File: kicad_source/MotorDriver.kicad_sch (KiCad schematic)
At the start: 44 parts, among them J7 x, J8 x, J9 x, Q1 2N7002, U4 74xx08, U5 IFX007T, U6 IFX007T, U7 IFX007T, U8 IFX007T

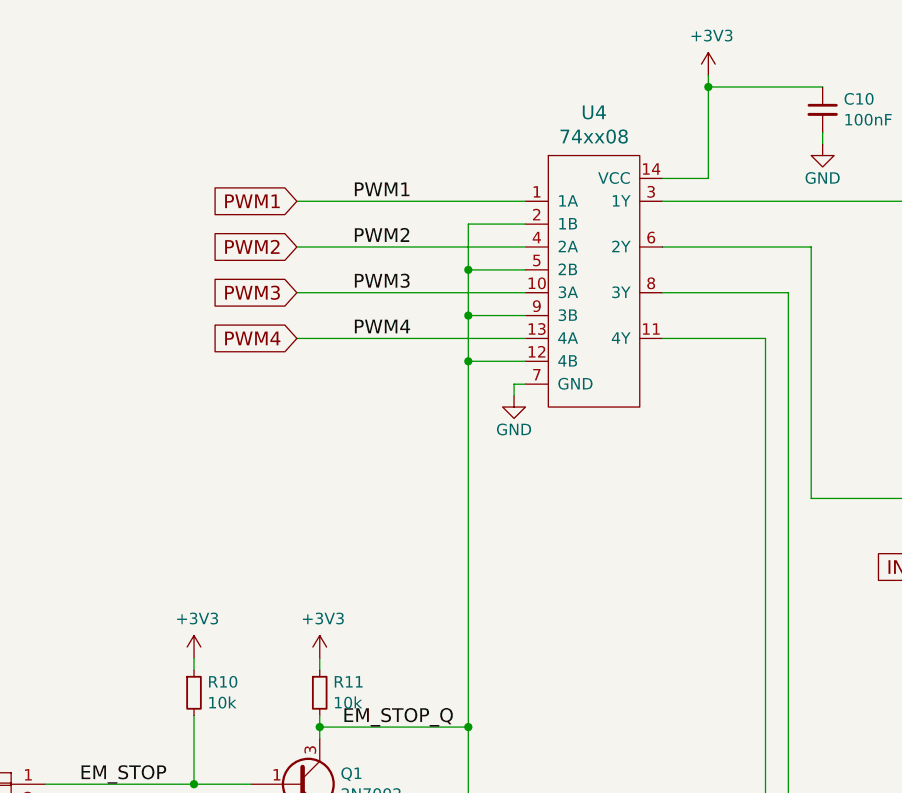
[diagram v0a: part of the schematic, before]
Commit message: combined 3.3V nets
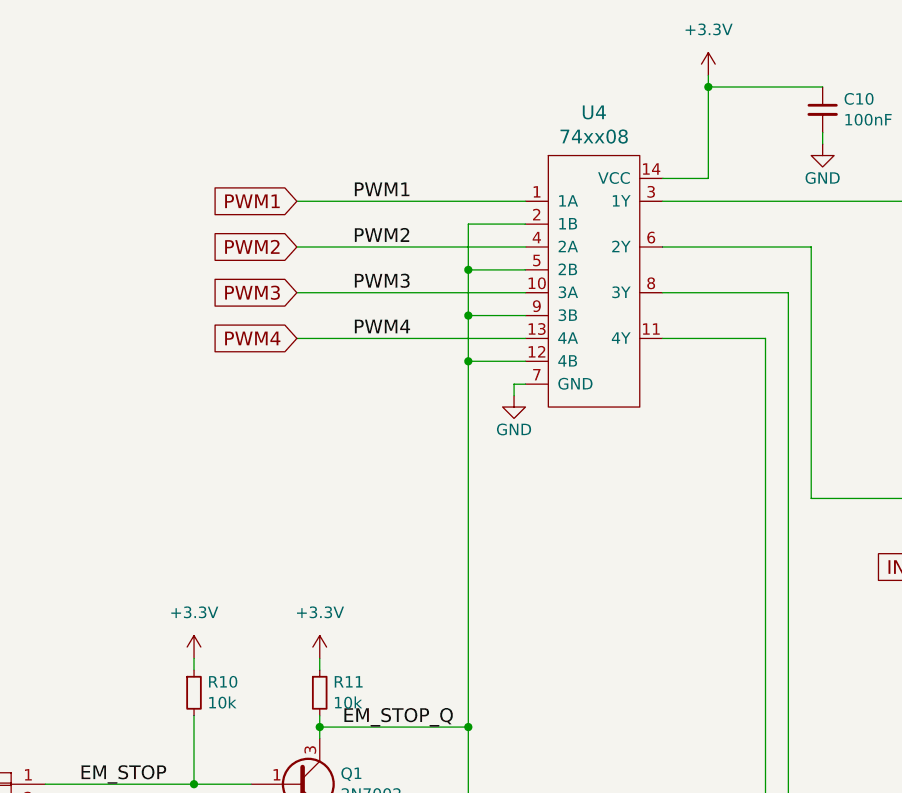
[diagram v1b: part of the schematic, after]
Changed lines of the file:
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@@
   (title_block
     (title "CyphalRobotController07/CAN")
-    (date "2023-11-15")
-    (rev "0.1")
+    (date "2023-12-03")
+    (rev "0.2")
     (company "generationmake")
     (comment 4 "This documentation describes Open Hardware and is licensed under the CERN OHL v. 1.2.")
@@
     (pin "1")
   )
-  (symbol (lib_id "power:+3.3V") (at 135.89 20.32 0) (unit 1)
-    (in_bom yes) (on_board yes)
-    (property "Reference" "#PWR048" (id 0) (at 135.89 24.13 0)
-      (effects (font (size 1.27 1.27)) hide)
-    )
-    (property "Value" "+3V3" (id 1) (at 136.271 15.9258 0))
-    (property "Footprint" "" (id 2) (at 135.89 20.32 0))
-    (property "Datasheet" "" (id 3) (at 135.89 20.32 0))
-    (pin "1")
-  )
   (symbol (lib_id "power:GND") (at 114.3 55.88 0) (unit 1)
     (in_bom yes) (on_board yes)
@@
     (pin "1")
   )
-  (symbol (lib_id "power:+3.3V") (at 92.71 85.09 0) (unit 1)
-    (in_bom yes) (on_board yes)
-    (property "Reference" "#PWR045" (id 0) (at 92.71 88.9 0)
-      (effects (font (size 1.27 1.27)) hide)
-    )
-    (property "Value" "+3V3" (id 1) (at 93.091 80.6958 0))
-    (property "Footprint" "" (id 2) (at 92.71 85.09 0))
-    (property "Datasheet" "" (id 3) (at 92.71 85.09 0))
-    (pin "1")
-  )
-  (symbol (lib_id "power:+3.3V") (at 78.74 85.09 0) (unit 1)
-    (in_bom yes) (on_board yes)
-    (property "Reference" "#PWR044" (id 0) (at 78.74 88.9 0)
-      (effects (font (size 1.27 1.27)) hide)
-    )
-    (property "Value" "+3V3" (id 1) (at 79.121 80.6958 0))
-    (property "Footprint" "" (id 2) (at 78.74 85.09 0))
-    (property "Datasheet" "" (id 3) (at 78.74 85.09 0))
-    (pin "1")
-  )
   (symbol (lib_id "OpenCyphalRobotController07-rescue:WR-TBL_691313710002-mechanical-connectors") (at 57.15 100.33 0) (mirror y) (unit 1)
     (in_bom yes) (on_board yes)
@@
     (pin "1")
   )
+  (symbol (lib_id "power:+3.3V") (at 92.71 85.09 0) (unit 1)
+    (in_bom yes) (on_board yes) (fields_autoplaced)
+    (property "Reference" "#PWR0134" (id 0) (at 92.71 88.9 0)
+      (effects (font (size 1.27 1.27)) hide)
+    )
+    (property "Value" "+3.3V" (id 1) (at 92.71 80.01 0))
+    (property "Footprint" "" (id 2) (at 92.71 85.09 0)
+      (effects (font (size 1.27 1.27)) hide)
+    )
+    (property "Datasheet" "" (id 3) (at 92.71 85.09 0)
+      (effects (font (size 1.27 1.27)) hide)
+    )
+    (pin "1")
+  )
   (symbol (lib_id "power:+BATT") (at 67.31 140.97 0) (unit 1)
     (in_bom yes) (on_board yes) (fields_autoplaced)
@@
     (pin "1")
   )
+  (symbol (lib_id "power:+3.3V") (at 78.74 85.09 0) (unit 1)
+    (in_bom yes) (on_board yes) (fields_autoplaced)
+    (property "Reference" "#PWR0101" (id 0) (at 78.74 88.9 0)
+      (effects (font (size 1.27 1.27)) hide)
+    )
+    (property "Value" "+3.3V" (id 1) (at 78.74 80.01 0))
+    (property "Footprint" "" (id 2) (at 78.74 85.09 0)
+      (effects (font (size 1.27 1.27)) hide)
+    )
+    (property "Datasheet" "" (id 3) (at 78.74 85.09 0)
+      (effects (font (size 1.27 1.27)) hide)
+    )
+    (pin "1")
+  )
   (symbol (lib_id "power:+BATT") (at 50.8 140.97 0) (unit 1)
     (in_bom yes) (on_board yes) (fields_autoplaced)
@@
       (effects (font (size 1.27 1.27)) hide)
     )
+    (pin "1")
+  )
+  (symbol (lib_id "power:+3.3V") (at 135.89 20.32 0) (unit 1)
+    (in_bom yes) (on_board yes) (fields_autoplaced)
+    (property "Reference" "#PWR0136" (id 0) (at 135.89 24.13 0)
+      (effects (font (size 1.27 1.27)) hide)
+    )
+    (property "Value" "+3.3V" (id 1) (at 135.89 15.24 0))
+    (property "Footprint" "" (id 2) (at 135.89 20.32 0)
+      (effects (font (size 1.27 1.27)) hide)
+    )
+    (property "Datasheet" "" (id 3) (at 135.89 20.32 0)
+      (effects (font (size 1.27 1.27)) hide)
+    )

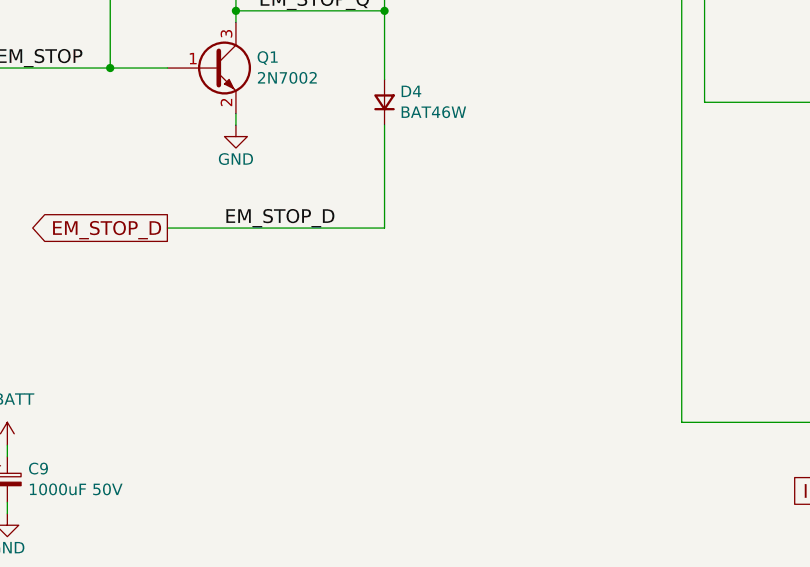
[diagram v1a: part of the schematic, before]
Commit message: added weak pull down on EM_STOP_D
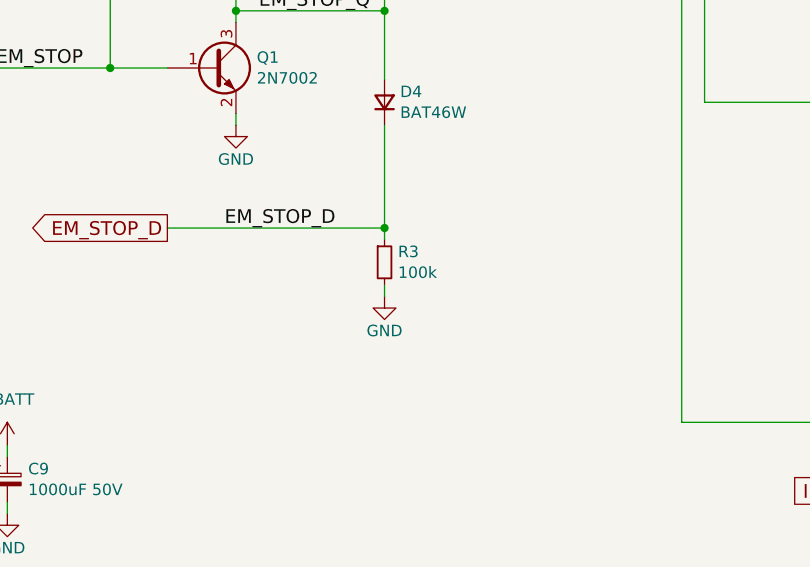
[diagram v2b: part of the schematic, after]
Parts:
- added R3: 100k, Resistor_SMD:R_0603_1608Metric, symbol Device:R_Small
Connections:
- net EM_STOP_D: now also R3.1
- net GND: now also R3.2
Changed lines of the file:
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@@
   (junction (at 92.71 92.71) (diameter 0) (color 0 0 0 0)
   )
+  (junction (at 109.22 116.84) (diameter 0) (color 0 0 0 0)
+  )
   (junction (at 189.23 149.86) (diameter 0) (color 0 0 0 0)
   )
@@
     (stroke (width 0) (type default) (color 0 0 0 0))
   )
+  (wire (pts (xy 109.22 123.19) (xy 109.22 124.46))
+    (stroke (width 0) (type default) (color 0 0 0 0))
+  )
   (wire (pts (xy 245.11 50.8) (xy 247.65 50.8))
     (stroke (width 0) (type default) (color 0 0 0 0))
@@
   )
   (wire (pts (xy 135.89 21.59) (xy 135.89 31.75))
+    (stroke (width 0) (type default) (color 0 0 0 0))
+  )
+  (wire (pts (xy 109.22 116.84) (xy 109.22 118.11))
     (stroke (width 0) (type default) (color 0 0 0 0))
   )
@@
     (pin "1")
   )
+  (symbol (lib_id "power:GND") (at 109.22 124.46 0) (unit 1)
+    (in_bom yes) (on_board yes)
+    (property "Reference" "#PWR020" (id 0) (at 109.22 130.81 0)
+      (effects (font (size 1.27 1.27)) hide)
+    )
+    (property "Value" "GND" (id 1) (at 109.22 128.27 0))
+    (property "Footprint" "" (id 2) (at 109.22 124.46 0))
+    (property "Datasheet" "" (id 3) (at 109.22 124.46 0))
+    (pin "1")
+  )
+  (symbol (lib_id "Device:R_Small") (at 109.22 120.65 0) (unit 1)
+    (in_bom yes) (on_board yes)
+    (property "Reference" "R3" (id 0) (at 110.7186 119.4816 0)
+      (effects (font (size 1.27 1.27)) (justify left))
+    )
+    (property "Value" "100k" (id 1) (at 110.7186 121.793 0)
+      (effects (font (size 1.27 1.27)) (justify left))
+    )
+    (property "Footprint" "Resistor_SMD:R_0603_1608Metric" (id 2) (at 109.22 124.46 0)
+      (effects (font (size 1.27 1.27)) hide)
+    )
+    (property "Datasheet" "" (id 3) (at 109.22 120.65 0))
+    (pin "1")
+    (pin "2")
+  )
   (symbol (lib_id "power:+3.3V") (at 78.74 85.09 0) (unit 1)

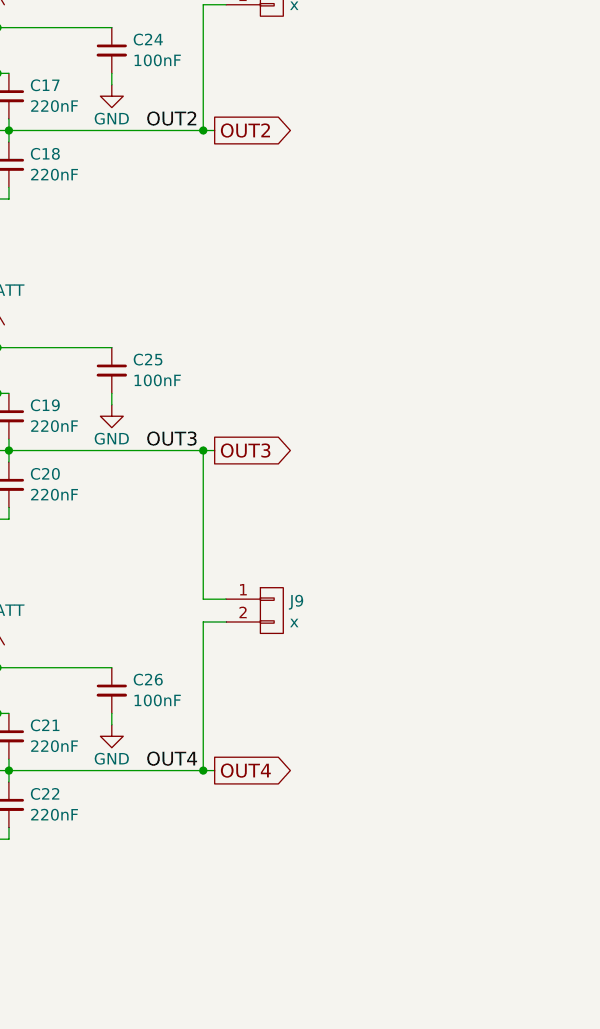
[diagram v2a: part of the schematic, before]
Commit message: added JST XH connector for motor and encoder
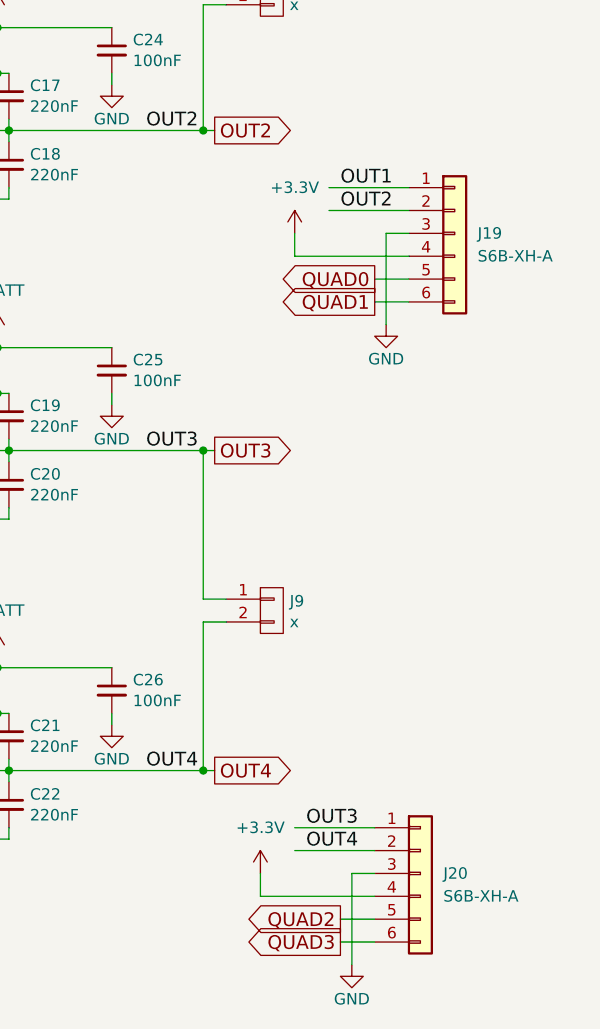
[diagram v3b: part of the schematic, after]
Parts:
- added J19, J20: S6B-XH-A, Connector_JST:JST_XH_S6B-XH-A_1x06_P2.50mm_Horizontal, symbol Connector_Generic:Conn_01x06
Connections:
- net +3.3V: now also J19.4 (Pin_4), J20.4 (Pin_4)
- net GND: now also J19.3 (Pin_3), J20.3 (Pin_3)
- net OUT1: now also J19.1 (Pin_1)
- net OUT2: now also J19.2 (Pin_2)
- net OUT3: now also J20.1 (Pin_1)
- net OUT4: now also J20.2 (Pin_2)
- new net QUAD0: J19.5 (Pin_5)
- new net QUAD1: J19.6 (Pin_6)
- new net QUAD2: J20.5 (Pin_5)
- new net QUAD3: J20.6 (Pin_6)

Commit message: changed motor connector, connected encoder
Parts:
- J8, J9: footprint Connector_Phoenix_MC:PhoenixContact_MC_1,5_2-G-3.81_1x02_P3.81mm_Horizontal -> Connector_Phoenix_MSTB:PhoenixContact_MSTBA_2,5_2-G-5,08_1x02_P5.08mm_Horizontal
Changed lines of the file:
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@@
   (title_block
     (title "CyphalRobotController07/CAN")
-    (date "2023-12-03")
+    (date "2024-01-04")
     (rev "0.2")
     (company "generationmake")
@@
       (effects (font (size 1.27 1.27)) (justify left))
     )
-    (property "Footprint" "Connector_Phoenix_MC:PhoenixContact_MC_1,5_2-G-3.81_1x02_P3.81mm_Horizontal" (id 2) (at 250.19 50.8 0)
+    (property "Footprint" "Connector_Phoenix_MSTB:PhoenixContact_MSTBA_2,5_2-G-5,08_1x02_P5.08mm_Horizontal" (id 2) (at 250.19 50.8 0)
       (effects (font (size 1.27 1.27)) hide)
     )
@@
       (effects (font (size 1.27 1.27)) (justify left))
     )
-    (property "Footprint" "Connector_Phoenix_MC:PhoenixContact_MC_1,5_2-G-3.81_1x02_P3.81mm_Horizontal" (id 2) (at 250.19 119.38 0)
-      (effects (font (size 1.27 1.27)) hide)
-    )
+    (property "Footprint" "Connector_Phoenix_MSTB:PhoenixContact_MSTBA_2,5_2-G-5,08_1x02_P5.08mm_Horizontal" (id 2) (at 250.19 119.38 0)
+      (effects (font (size 1.27 1.27)) hide)
+    )

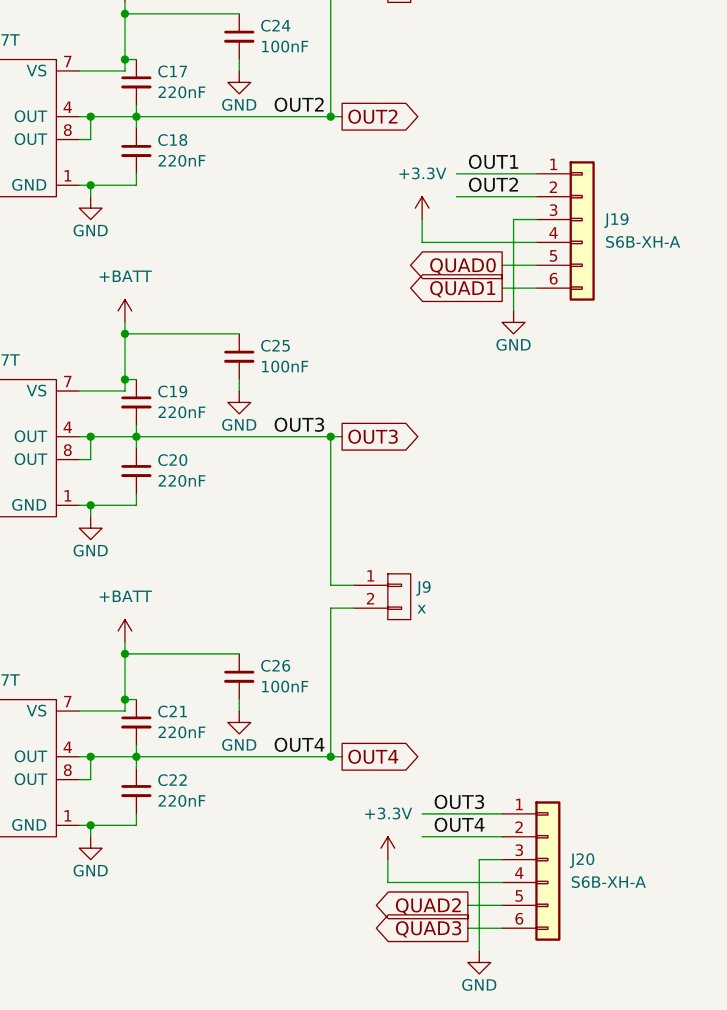
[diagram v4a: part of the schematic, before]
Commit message: finished layout near encoder level converter
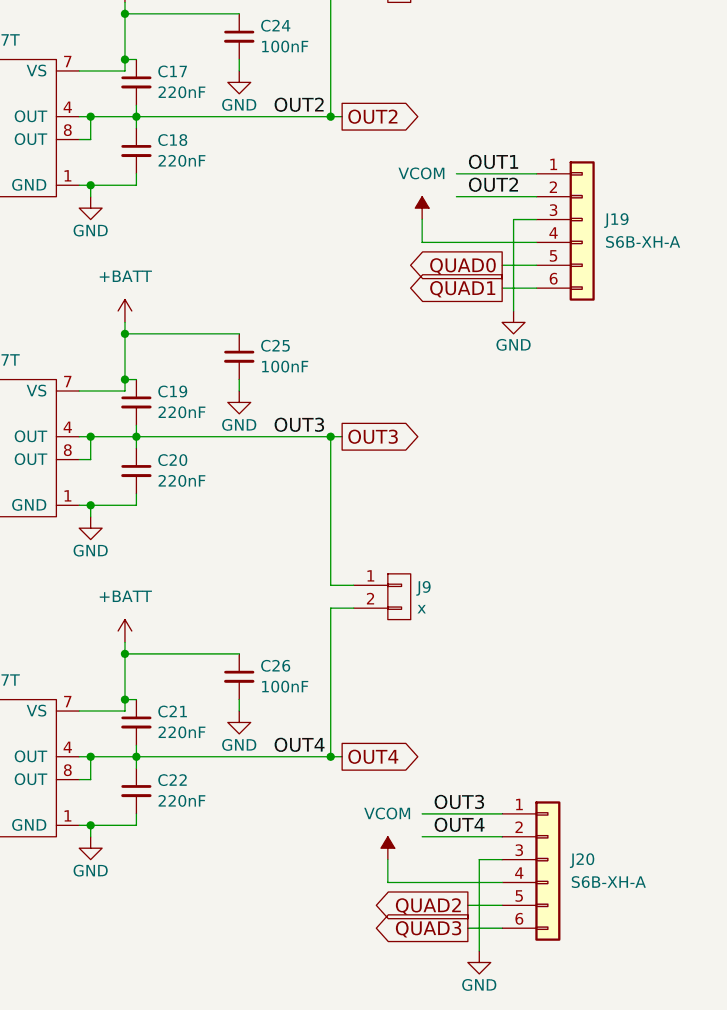
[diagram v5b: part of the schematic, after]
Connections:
- net +3.3V: no longer J19.4 (Pin_4), J20.4 (Pin_4)
- new net VCOM: J19.4 (Pin_4), J20.4 (Pin_4)
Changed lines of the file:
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@@
+    (pin "1")
+  )
+  (symbol (lib_id "power:VCOM") (at 251.46 149.86 0) (unit 1)
+    (in_bom yes) (on_board yes) (fields_autoplaced)
+    (property "Reference" "#PWR?" (id 0) (at 251.46 153.67 0)
+      (effects (font (size 1.27 1.27)) hide)
+    )
+    (property "Value" "VCOM" (id 1) (at 251.46 144.78 0))
+    (property "Footprint" "" (id 2) (at 251.46 149.86 0)
+      (effects (font (size 1.27 1.27)) hide)
+    )
+    (property "Datasheet" "" (id 3) (at 251.46 149.86 0)
+      (effects (font (size 1.27 1.27)) hide)
+    )
     (pin "1")
   )
@@
     (pin "1")
   )
-  (symbol (lib_id "power:+3.3V") (at 255.27 78.74 0) (unit 1)
+  (symbol (lib_id "power:VCOM") (at 255.27 78.74 0) (unit 1)
     (in_bom yes) (on_board yes) (fields_autoplaced)
-    (property "Reference" "#PWR044" (id 0) (at 255.27 82.55 0)
+    (property "Reference" "#PWR?" (id 0) (at 255.27 82.55 0)
       (effects (font (size 1.27 1.27)) hide)
     )
-    (property "Value" "+3.3V" (id 1) (at 255.27 73.66 0))
+    (property "Value" "VCOM" (id 1) (at 255.27 73.66 0))
     (property "Footprint" "" (id 2) (at 255.27 78.74 0)
       (effects (font (size 1.27 1.27)) hide)
@@
     (pin "2")
   )
-  (symbol (lib_id "power:+3.3V") (at 251.46 149.86 0) (unit 1)
-    (in_bom yes) (on_board yes) (fields_autoplaced)
-    (property "Reference" "#PWR048" (id 0) (at 251.46 153.67 0)
-      (effects (font (size 1.27 1.27)) hide)
-    )
-    (property "Value" "+3.3V" (id 1) (at 251.46 144.78 0))
-    (property "Footprint" "" (id 2) (at 251.46 149.86 0)
-      (effects (font (size 1.27 1.27)) hide)
-    )
-    (property "Datasheet" "" (id 3) (at 251.46 149.86 0)
-      (effects (font (size 1.27 1.27)) hide)
-    )
-    (pin "1")
-  )
   (symbol (lib_id "power:GND") (at 261.62 160.02 0) (unit 1)

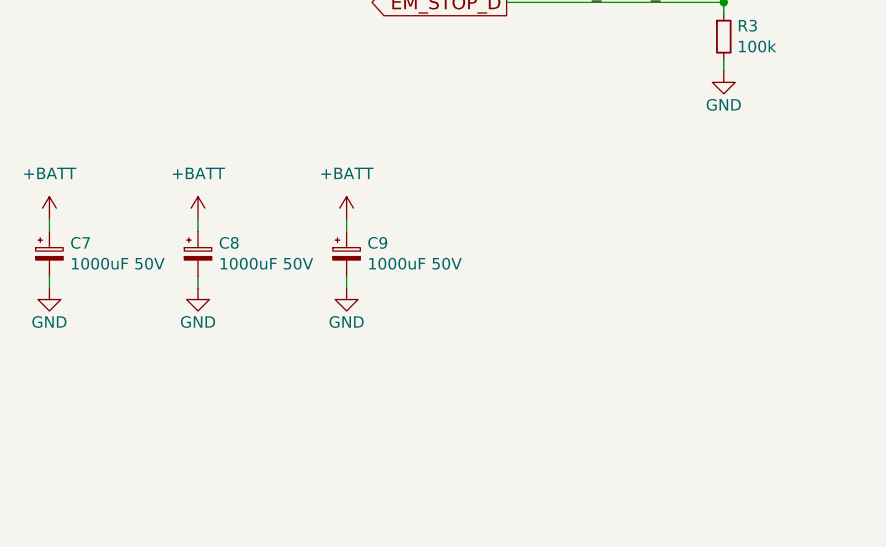
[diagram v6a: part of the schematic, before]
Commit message: replaced tantal with electrolytic capacitors
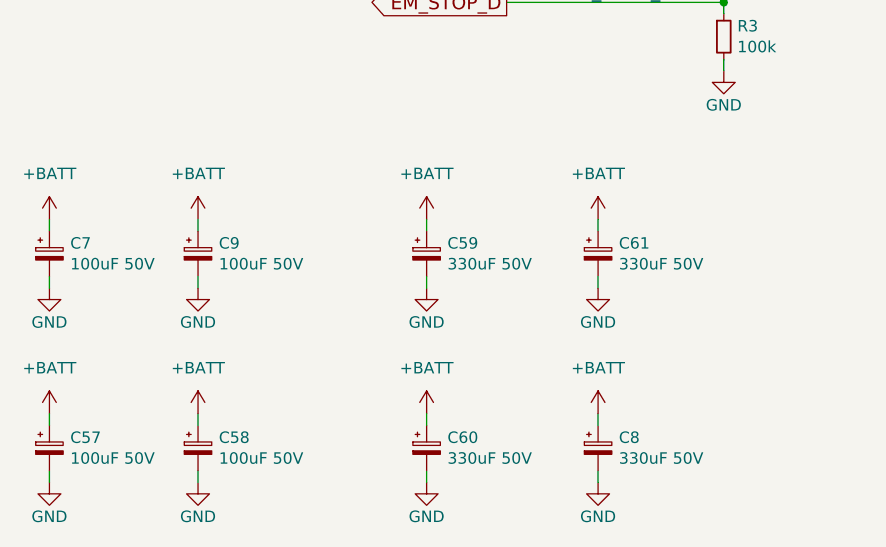
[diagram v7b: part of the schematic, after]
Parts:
- added C57, C58: 100uF 50V, Capacitor_SMD:CP_Elec_6.3x7.7, symbol Device:C_Polarized_Small
- added C59, C60, C61: 330uF 50V, Capacitor_SMD:CP_Elec_10x12.5, symbol Device:C_Polarized_Small
- C7, C9: value 1000uF 50V -> 100uF 50V; footprint Capacitor_THT:CP_Radial_D16.0mm_P7.50mm -> Capacitor_SMD:CP_Elec_6.3x7.7
- C8: value 1000uF 50V -> 330uF 50V; footprint Capacitor_THT:CP_Radial_D16.0mm_P7.50mm -> Capacitor_SMD:CP_Elec_10x12.5
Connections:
- net +BATT: now also C57.1, C58.1, C59.1, C60.1, C61.1
- net GND: now also C57.2, C58.2, C59.2, C60.2, C61.2
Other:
- moved on the sheet: C8, C9
